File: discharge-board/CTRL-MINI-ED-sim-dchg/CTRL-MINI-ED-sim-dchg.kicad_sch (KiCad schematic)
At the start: 36 parts, among them Q2 NPN, U1 Opamp_Dual, U3 Opamp_Dual

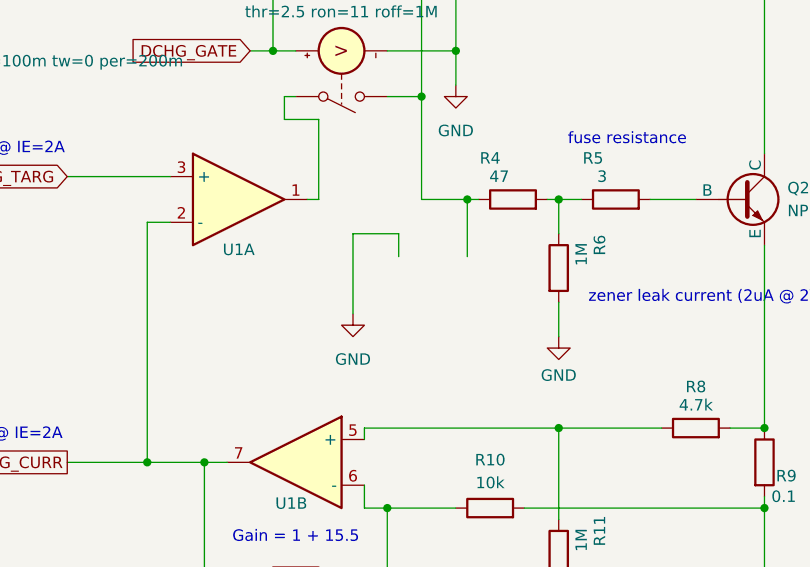
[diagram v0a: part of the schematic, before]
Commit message: Update ED (current sensor, output protection diode) based on sims
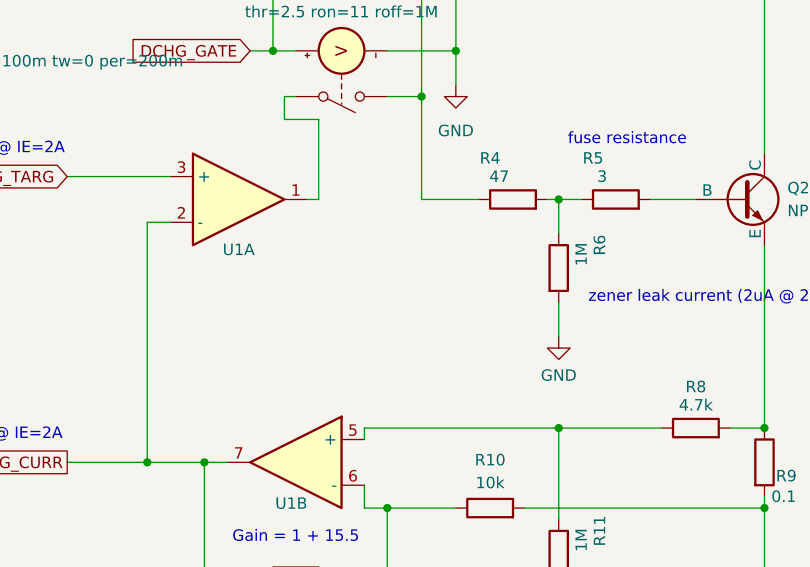
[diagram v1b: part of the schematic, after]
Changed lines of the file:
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@@
-	)
-	(junction
-		(at 182.88 76.2)
-		(diameter 0)
-		(color 0 0 0 0)
 	)
 	(junction
@@
 	(wire
 		(pts
-			(xy 175.26 80.01) (xy 175.26 82.55)
-		)
-		(stroke
-			(width 0)
-			(type default)
-		)
-	)
-	(wire
-		(pts
 			(xy 177.8 64.77) (xy 177.8 76.2)
 		)
@@
 	(wire
 		(pts
-			(xy 177.8 76.2) (xy 182.88 76.2)
-		)
-		(stroke
-			(width 0)
-			(type default)
-		)
-	)
-	(wire
-		(pts
 			(xy 156.21 105.41) (xy 153.67 105.41)
 		)
@@
 	(wire
 		(pts
-			(xy 182.88 76.2) (xy 182.88 82.55)
-		)
-		(stroke
-			(width 0)
-			(type default)
-		)
-	)
-	(wire
-		(pts
 			(xy 166.37 67.31) (xy 166.37 76.2)
 		)
@@
 	(wire
 		(pts
-			(xy 170.18 80.01) (xy 175.26 80.01)
-		)
-		(stroke
-			(width 0)
-			(type default)
-		)
-	)
-	(wire
-		(pts
 			(xy 30.48 162.56) (xy 67.31 162.56)
 		)
@@
 	(wire
 		(pts
-			(xy 182.88 76.2) (xy 184.15 76.2)
+			(xy 177.8 76.2) (xy 184.15 76.2)
 		)
 		(stroke
@@
 		(pts
 			(xy 58.42 45.72) (xy 58.42 55.88)
-		)
-		(stroke
-			(width 0)
-			(type default)
-		)
-	)
-	(wire
-		(pts
-			(xy 170.18 80.01) (xy 170.18 88.9)
 		)
 		(stroke
@@
 					(unit 1)
 				)
-			)
-		)
-	)
-	(symbol
-		(lib_id "power:GND")
-		(at 170.18 88.9 0)
-		(unit 1)
-		(exclude_from_sim no)
-		(in_bom yes)
-		(on_board yes)
-		(dnp no)
-		(fields_autoplaced yes)
-		(property "Reference" "#PWR06"
-			(at 170.18 95.25 0)
-			(effects
-				(font
-					(size 1.27 1.27)
-				)
-				(hide yes)
-			)
-		)
-		(property "Value" "GND"
-			(at 170.18 93.98 0)
-			(effects
-				(font
-					(size 1.27 1.27)
-				)
-			)
-		)
-		(property "Footprint" ""
-			(at 170.18 88.9 0)
-			(effects
-				(font
-					(size 1.27 1.27)
-				)
-				(hide yes)
-			)
-		)
-		(property "Datasheet" ""
-			(at 170.18 88.9 0)
-			(effects
-				(font
-					(size 1.27 1.27)
-				)
-				(hide yes)
-			)
-		)
-		(property "Description" "Power symbol creates a global label with name \"GND\" , ground"
-			(at 170.18 88.9 0)
-			(effects
-				(font
-					(size 1.27 1.27)
-				)
-				(hide yes)
-			)
-		)
-		(pin "1"
-		)
-		(instances
-			(project "CTRL-MINI-ED"
-				(path "/3fa1ca74-4d0d-40dd-8b5c-0d4be11bd5b5"
-					(reference "#PWR06")
-					(unit 1)
-				)

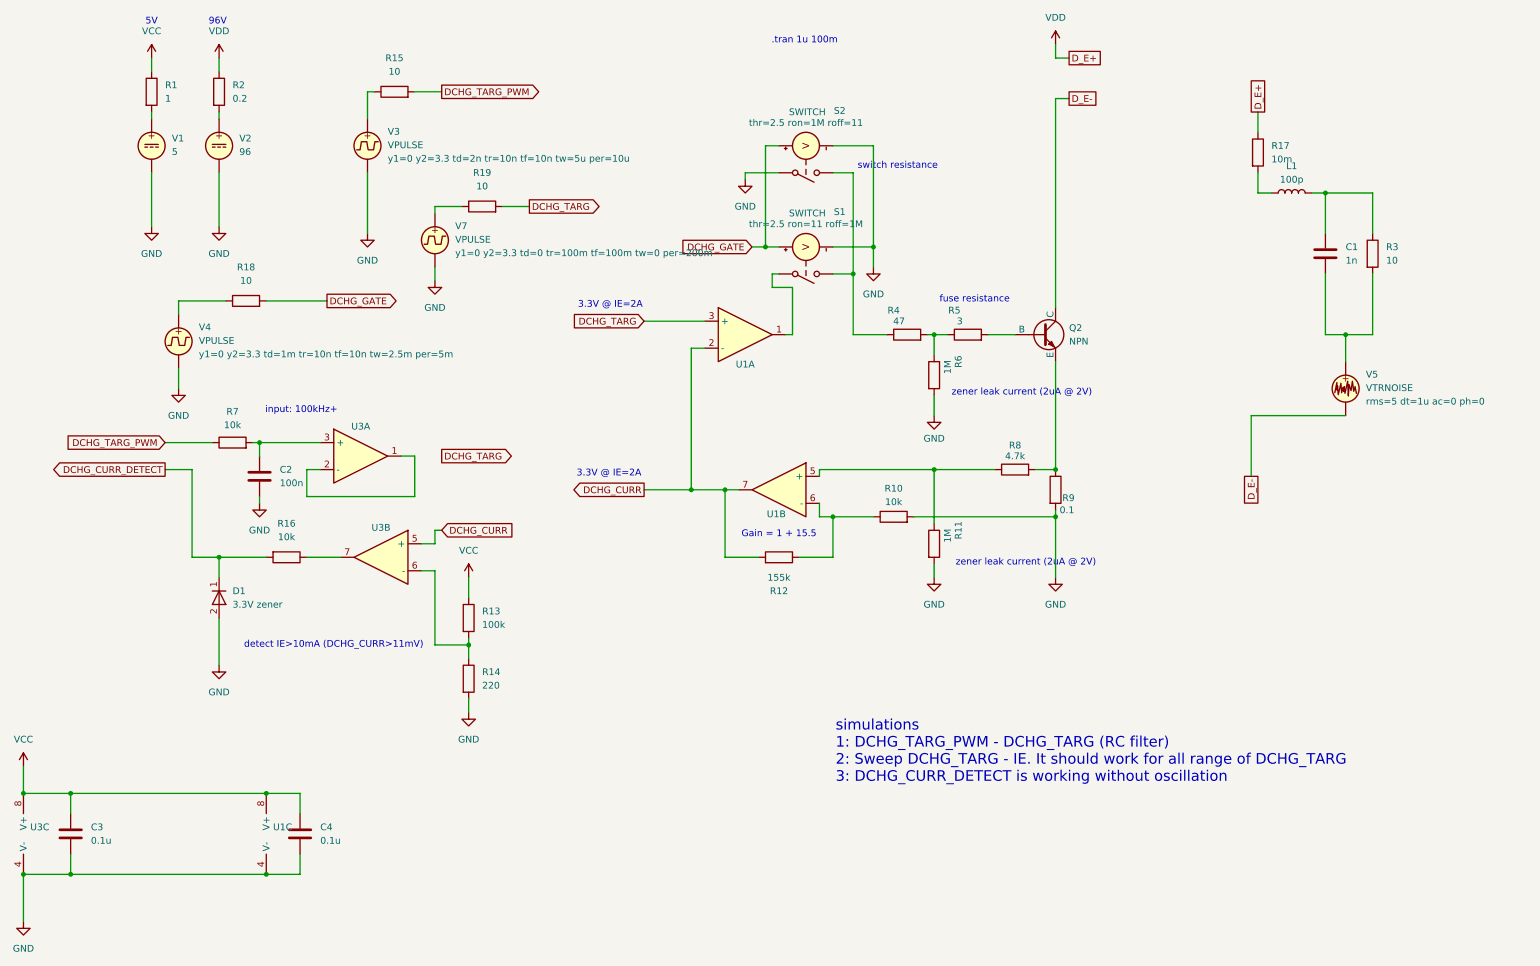
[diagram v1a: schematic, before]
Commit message: CTRL-MINI-ED r1 draft schematics
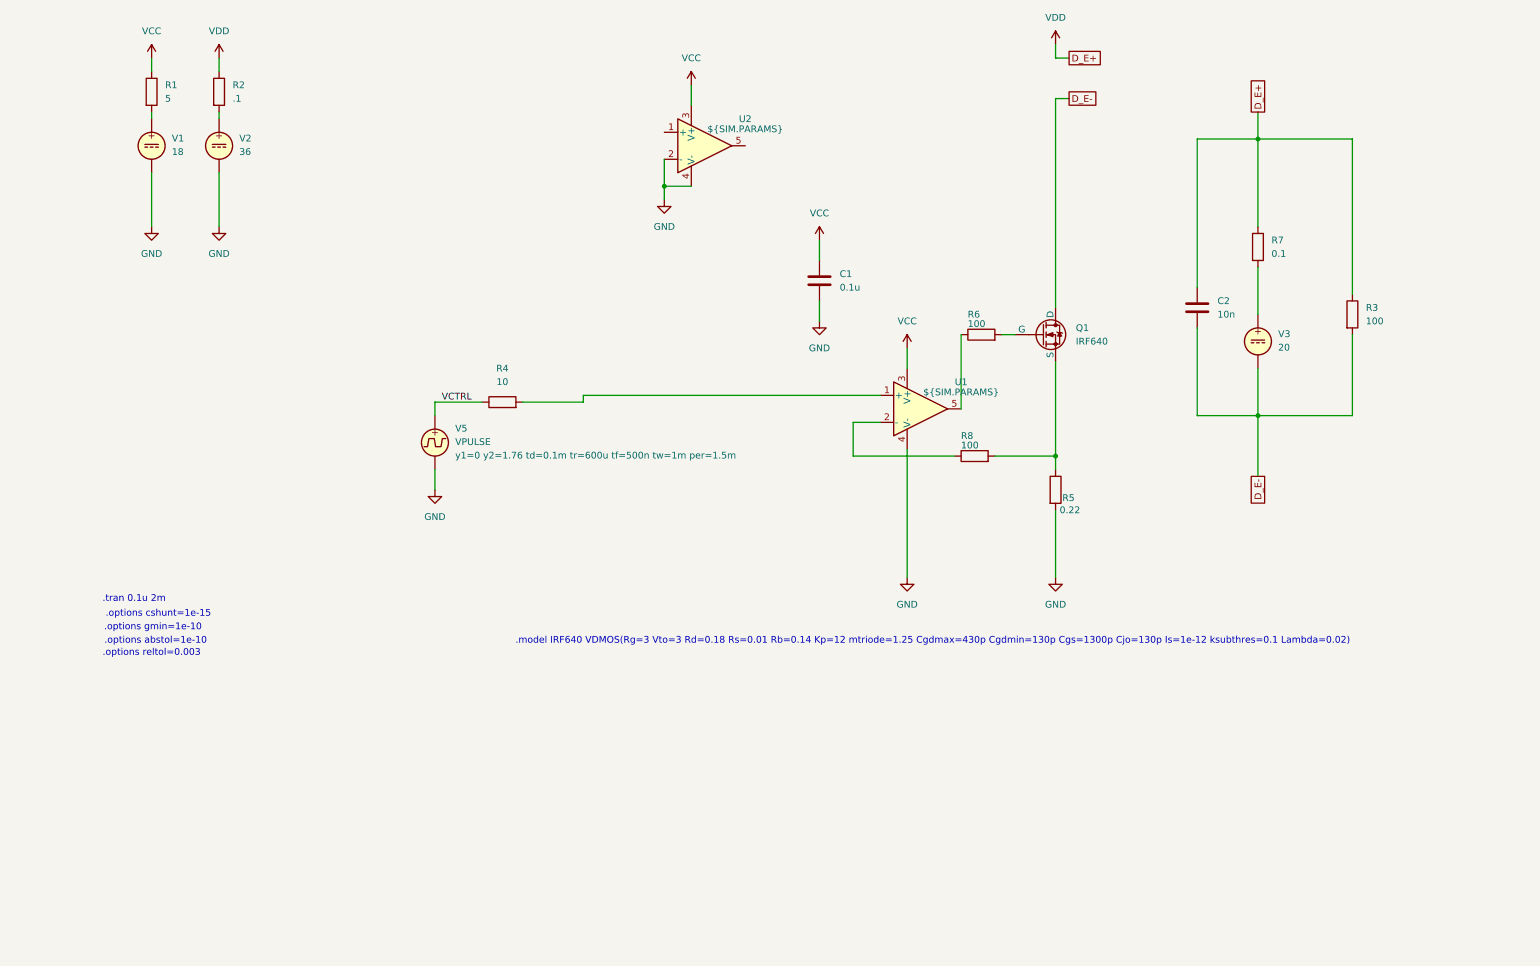
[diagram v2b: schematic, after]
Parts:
- removed C3, C4: 0.1u, Capacitor_SMD:C_0603_1608Metric, symbol Device:C
- removed D1: 3.3V zener, symbol Simulation_SPICE:D
- removed L1: 100p, symbol Device:L
- removed Q2: NPN, symbol Simulation_SPICE:NPN
- removed R10, R16: 10k, Resistor_SMD:R_0603_1608Metric, symbol Device:R
- removed R11: 1M, Resistor_SMD:R_0603_1608Metric, symbol Device:R
- removed R12: 155k, Resistor_SMD:R_0603_1608Metric, symbol Device:R
- removed R13: 100k, Resistor_SMD:R_0603_1608Metric, symbol Device:R
- removed R14: 220, Resistor_SMD:R_0603_1608Metric, symbol Device:R
- removed R15, R19: 10, symbol Device:R
- removed R17: 10m, symbol Device:R
- removed R4: 47, Resistor_SMD:R_0603_1608Metric, symbol Device:R
- removed R5: 3, Resistor_SMD:R_0603_1608Metric, symbol Device:R
- removed S1, S2: SWITCH, symbol Simulation_SPICE:SWITCH
- removed U1, U3: Opamp_Dual, Package_SO:VSSOP-8_3x3mm_P0.65mm, symbol Device:Opamp_Dual
- removed V3, V7: VPULSE, symbol Simulation_SPICE:VPULSE
- removed V5: VTRNOISE, symbol Simulation_SPICE:VTRNOISE
- added Q1: IRF640, symbol Simulation_SPICE:NMOS
- added U1, U2: ${SIM.PARAMS}, symbol Simulation_SPICE:OPAMP
- added V3: 20, symbol Simulation_SPICE:VDC
- C1: value 1n -> 0.1u; footprint (none) -> Capacitor_SMD:C_0603_1608Metric
- C2: value 100n -> 10n; footprint Capacitor_SMD:C_0603_1608Metric -> (none)
- R1: value 1 -> 5
- R2: value 0.2 -> .1
- R3: value 10 -> 100
- R5: renamed from R9; value 0.1 -> 0.22
- R6: value 1M -> 100
- R7: value 10k -> 0.1; footprint Resistor_SMD:R_0603_1608Metric -> (none)
- R8: value 4.7k -> 100
- V1: value 5 -> 18
- V2: value 96 -> 36
- renumbered R18 to R4, V4 to V5
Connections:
- net DCHG_TARG_PWM is gone; now on net VDD: R7.1
- net D_E-: now also C2.2, R3.2, Q1.1 (D), V3.2
- net GND: now also C1.2, U1.4 (V-), U2.2 (-), U2.4 (V-); no longer C2.2, R6.2
- net VCC: now also C1.1, U1.3 (V+), U2.3 (V+)
- net VDD: now also C2.1, R3.1
- net at R6.1: now also U1.5
- net at R5.1, R8.2: now also Q1.3 (S)
- net at R8.1: now also U1.2 (-)
- net at R7.2: now also V3.1; no longer C2.1
- net VCTRL: now reaches R4.1, V5.1
- net DCHG_GATE: no longer names the net of R4.2
- net DCHG_GATE: now also U1.1 (+)
- new net: Q1.2 (G), R6.2
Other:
- note added: ".model IRF640 VDMOS(Rg=3 Vto=3 Rd=0.18 Rs=0.01 Rb=0.14 Kp=12 mtriode=1.25 Cgdmax=430p Cgdmin=130p Cgs=1300p Cjo=130p Is=1e-12 ksubthres=0.1 Lambda=0.02)"
- note added: ".options abstol=1e-10"
- note added: ".options cshunt=1e-15"
- note added: ".options gmin=1e-10"
- note added: ".options reltol=0.003"
- note added: ".tran 0.1u 2m"
- note removed: ".tran 1u 100m"
- note removed: "3.3V @ IE=2A"
- note removed: "5V"
- note removed: "96V"
- note removed: "Gain = 1 + 15.5"
- note removed: "detect IE>10mA (DCHG_CURR>11mV)"
- note removed: "fuse resistance"
- note removed: "input: 100kHz+"
- note removed: "simulations 1: DCHG_TARG_PWM - DCHG_TARG (RC filter) 2: Sweep DCHG_TARG - IE. It should work for all range of DCHG_TARG 3: DCHG_CURR_DETECT is working without oscillation"
- note removed: "switch resistance"
- note removed: "zener leak current (2uA @ 2V)"
- moved on the sheet: R4, V5
